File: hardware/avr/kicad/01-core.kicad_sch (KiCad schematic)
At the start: 13 parts, among them U1 ATmega1284P-PU, Y1 8MHz

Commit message: Fix malformed TestPoint library symbol
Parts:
- added TP_5V, TP_AREF, TP_AVCC, TP_GND, TP_RESET: TestPoint, symbol Connector:TestPoint
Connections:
- net +5V: now also TP_5V.1 (TestPoint)
- net AREF: now also TP_AREF.1 (TestPoint), TP_AVCC.1 (TestPoint), TP_GND.1 (TestPoint)
- net RESET: now also TP_RESET.1 (TestPoint)

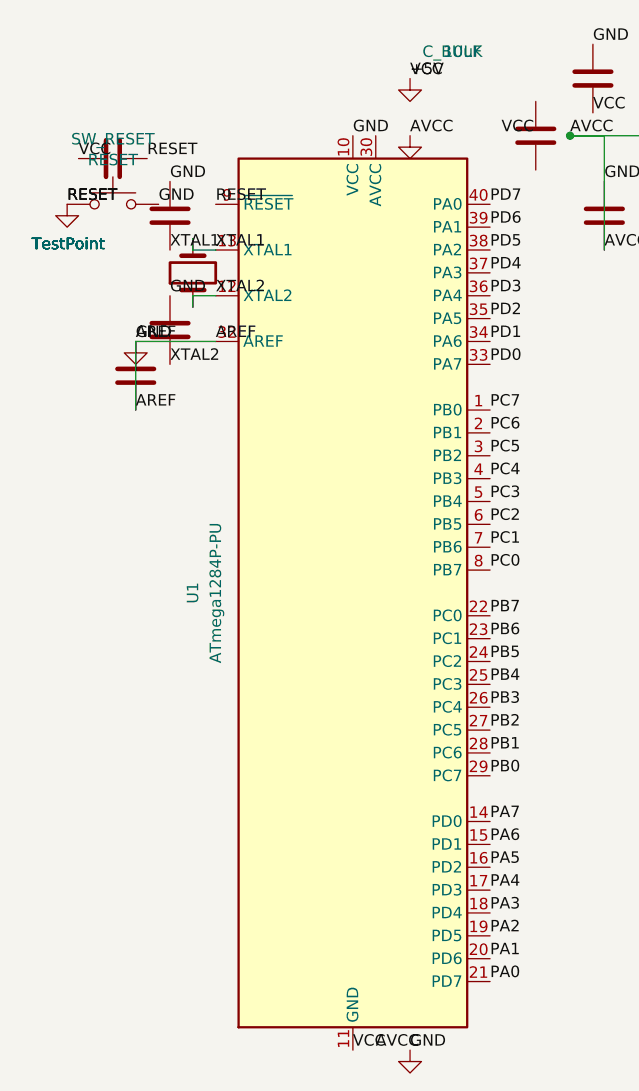
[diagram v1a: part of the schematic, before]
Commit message: Rebuild corrupted TestPoint library definition
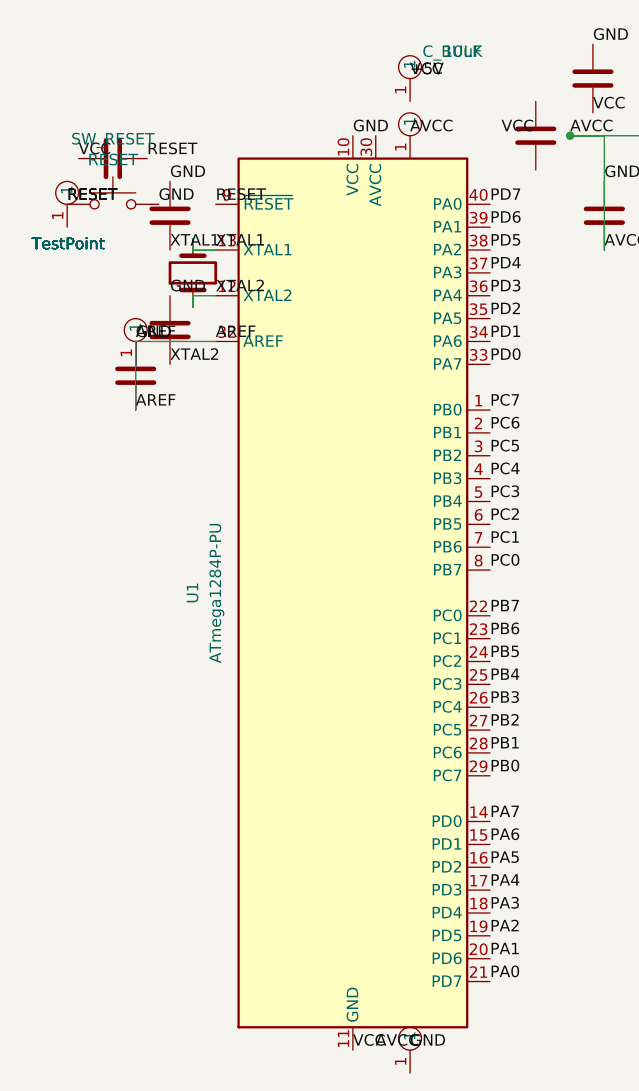
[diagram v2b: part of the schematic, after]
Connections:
- net +5V: no longer TP_5V.1 (TestPoint)
- net AREF: no longer TP_AREF.1 (TestPoint), TP_AVCC.1 (TestPoint), TP_GND.1 (TestPoint)
- net RESET: no longer TP_RESET.1 (TestPoint)
